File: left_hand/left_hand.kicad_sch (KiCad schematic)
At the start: 43 parts, among them J1 Conn_01x08, J2 Screw_Terminal_01x10, J3 8P8C_Shielded, J4 Conn_02x02_Top_Bottom, J7 Conn_01x02, J8 Conn_01x02, M1 Motor_Servo, M2 Motor_Servo, M3 Motor_Servo, M4 Motor_Servo, M5 Motor_Servo, Q1 Q_NMOS_GDS, Q2 Q_NMOS_GDS, Q3 Q_NMOS_GDS, Q4 Q_NMOS_GDS, Q5 Q_NMOS_GDS, U1 MCP23017_SP, U2 PCA9685PW

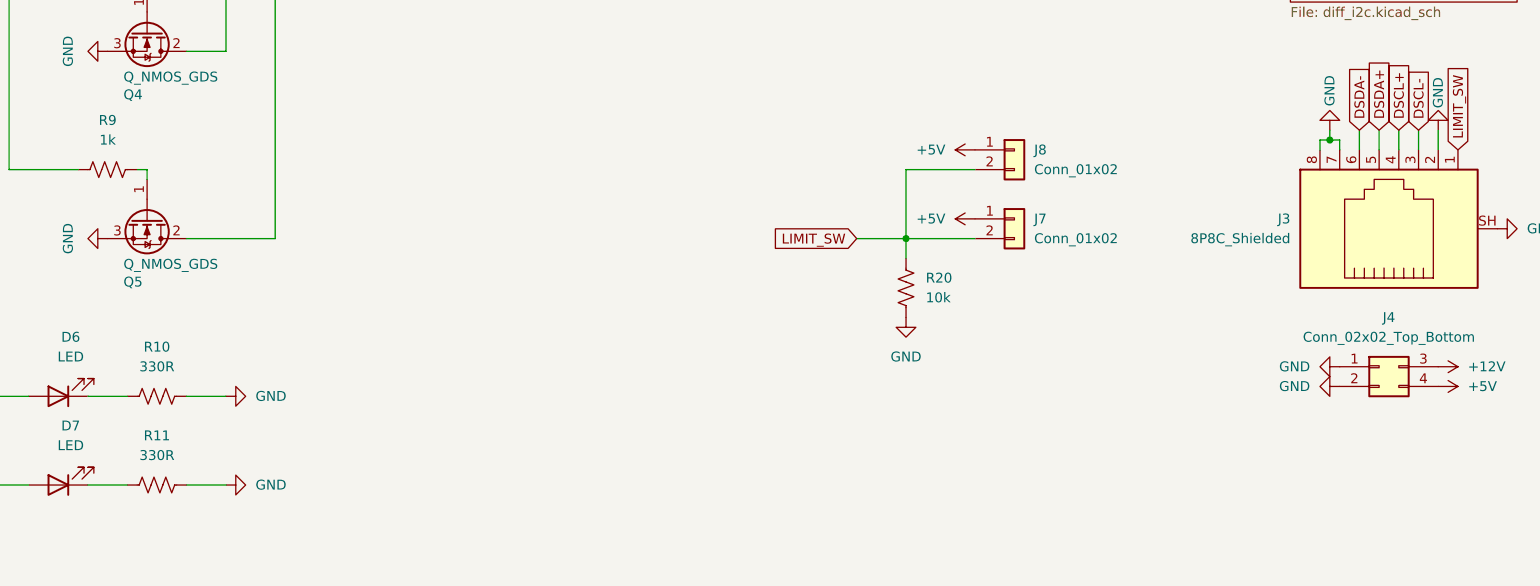
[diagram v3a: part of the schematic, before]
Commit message: Added screw terminals etc for both stepper drivers
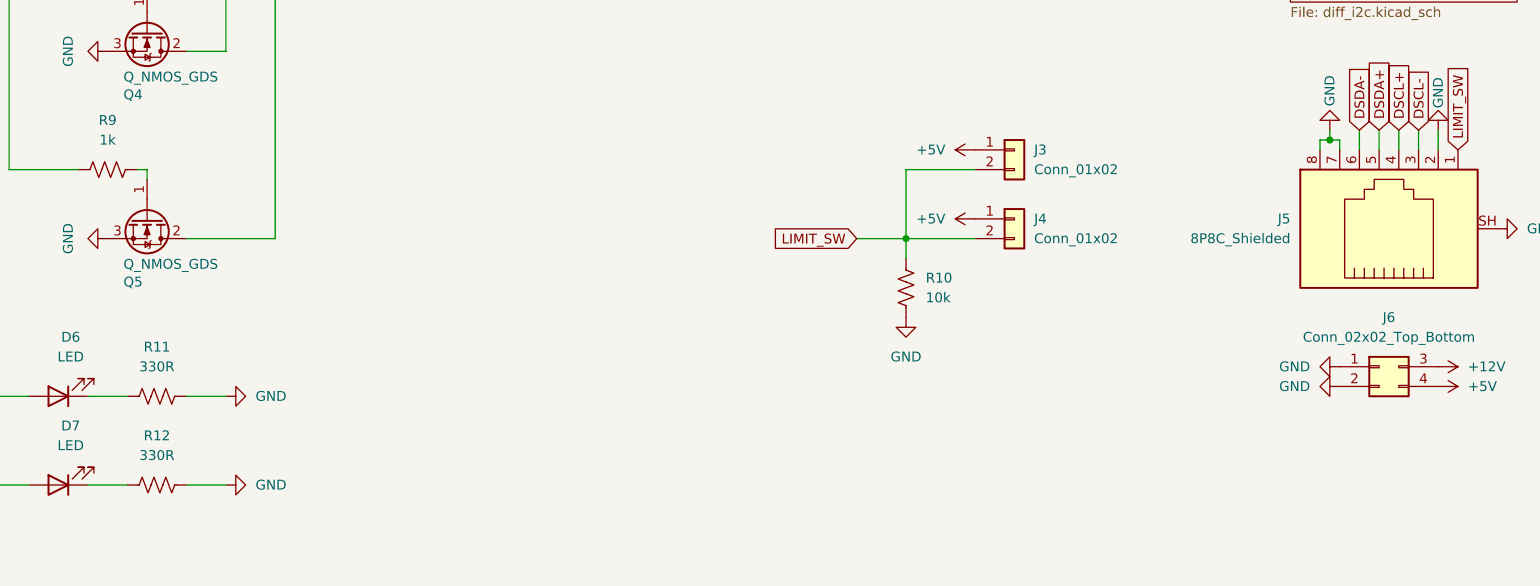
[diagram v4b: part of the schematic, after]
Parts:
- renumbered J8 to J3, J7 to J4, J3 to J5, J4 to J6, R20 to R10, R10 to R11, R11 to R12
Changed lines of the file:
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@@
 		(dnp no)
 		(fields_autoplaced yes)
-		(property "Reference" "#PWR036"
+		(property "Reference" "#PWR037"
 			(at 279.4 138.43 0)
 			(effects
@@
 			(project ""
 				(path "/22d0e2d6-ca63-4bde-b22b-39e933f56b8a"
-					(reference "#PWR036")
+					(reference "#PWR037")
 					(unit 1)
 				)
@@
 		(dnp no)
 		(fields_autoplaced yes)
-		(property "Reference" "#PWR021"
+		(property "Reference" "#PWR022"
 			(at 156.21 74.93 0)
 			(effects
@@
 			(project "left_hand"
 				(path "/22d0e2d6-ca63-4bde-b22b-39e933f56b8a"
-					(reference "#PWR021")
+					(reference "#PWR022")
 					(unit 1)
 				)
@@
 		(dnp no)
 		(fields_autoplaced yes)
-		(property "Reference" "#PWR055"
+		(property "Reference" "#PWR036"
 			(at 209.55 137.16 0)
 			(effects
@@
 			(project "left_hand"
 				(path "/22d0e2d6-ca63-4bde-b22b-39e933f56b8a"
-					(reference "#PWR055")
+					(reference "#PWR036")
 					(unit 1)
 				)
@@
 		(dnp no)
 		(fields_autoplaced yes)
-		(property "Reference" "#PWR040"
+		(property "Reference" "#PWR042"
 			(at 246.38 158.75 0)
 			(effects
@@
 			(project "left_hand"
 				(path "/22d0e2d6-ca63-4bde-b22b-39e933f56b8a"
-					(reference "#PWR040")
+					(reference "#PWR042")
 					(unit 1)
 				)
@@
 		(dnp no)
 		(fields_autoplaced yes)
-		(property "Reference" "J4"
+		(property "Reference" "J6"
 			(at 259.08 149.86 0)
 			(effects
@@
 			(project "left_hand"
 				(path "/22d0e2d6-ca63-4bde-b22b-39e933f56b8a"
-					(reference "J4")
+					(reference "J6")
 					(unit 1)
 				)
@@
 		(dnp no)
 		(fields_autoplaced yes)
-		(property "Reference" "#PWR038"
+		(property "Reference" "#PWR041"
 			(at 261.62 156.21 0)
 			(effects
@@
 			(project ""
 				(path "/22d0e2d6-ca63-4bde-b22b-39e933f56b8a"
-					(reference "#PWR038")
+					(reference "#PWR041")
 					(unit 1)
 				)
@@
 		(dnp no)
 		(fields_autoplaced yes)
-		(property "Reference" "#PWR057"
+		(property "Reference" "#PWR035"
 			(at 209.55 128.27 0)
 			(effects
@@
 			(project "left_hand"
 				(path "/22d0e2d6-ca63-4bde-b22b-39e933f56b8a"
-					(reference "#PWR057")
+					(reference "#PWR035")
 					(unit 1)
 				)
@@
 		(dnp no)
 		(fields_autoplaced yes)
-		(property "Reference" "#PWR023"
+		(property "Reference" "#PWR024"
 			(at 171.45 78.74 0)
 			(effects
@@
 			(project ""
 				(path "/22d0e2d6-ca63-4bde-b22b-39e933f56b8a"
-					(reference "#PWR023")
+					(reference "#PWR024")
 					(unit 1)
 				)
@@
 		(dnp no)
 		(fields_autoplaced yes)
-		(property "Reference" "R11"
+		(property "Reference" "R12"
 			(at 100.33 165.1 90)
 			(effects
@@
 			(project "left_hand"
 				(path "/22d0e2d6-ca63-4bde-b22b-39e933f56b8a"
-					(reference "R11")
+					(reference "R12")
 					(unit 1)
 				)
@@
 		(dnp no)
 		(fields_autoplaced yes)
-		(property "Reference" "#PWR035"
+		(property "Reference" "#PWR038"
 			(at 87.63 139.7 0)
 			(effects
@@
 			(project "left_hand"
 				(path "/22d0e2d6-ca63-4bde-b22b-39e933f56b8a"
-					(reference "#PWR035")
+					(reference "#PWR038")
 					(unit 1)
 				)
@@
 		(dnp no)
 		(fields_autoplaced yes)
-		(property "Reference" "J3"
+		(property "Reference" "J5"
 			(at 246.38 137.1599 90)
 			(effects
@@
 			(project ""
 				(path "/22d0e2d6-ca63-4bde-b22b-39e933f56b8a"
-					(reference "J3")
+					(reference "J5")
 					(unit 1)
 				)
@@
 		(dnp no)
 		(fields_autoplaced yes)
-		(property "Reference" "#PWR039"
+		(property "Reference" "#PWR044"
 			(at 115.57 160.02 0)
 			(effects
@@
 			(project "left_hand"
 				(path "/22d0e2d6-ca63-4bde-b22b-39e933f56b8a"
-					(reference "#PWR039")
+					(reference "#PWR044")
 					(unit 1)
 				)
@@
 		(dnp no)
 		(fields_autoplaced yes)
-		(property "Reference" "#PWR037"
+		(property "Reference" "#PWR040"
 			(at 246.38 156.21 0)
 			(effects
@@
 			(project "left_hand"
 				(path "/22d0e2d6-ca63-4bde-b22b-39e933f56b8a"
-					(reference "#PWR037")
+					(reference "#PWR040")
 					(unit 1)
 				)
@@
 		(dnp no)
 		(fields_autoplaced yes)
-		(property "Reference" "#PWR020"
+		(property "Reference" "#PWR021"
 			(at 87.63 67.31 0)
 			(effects
@@
 			(project "left_hand"
 				(path "/22d0e2d6-ca63-4bde-b22b-39e933f56b8a"
-					(reference "#PWR020")
+					(reference "#PWR021")
 					(unit 1)
 				)
@@
 		(on_board yes)
 		(dnp no)
-		(property "Reference" "#PWR042"
+		(property "Reference" "#PWR045"
 			(at 115.57 171.45 0)
 			(effects
@@
 			(project "left_hand"
 				(path "/22d0e2d6-ca63-4bde-b22b-39e933f56b8a"
-					(reference "#PWR042")
+					(reference "#PWR045")
 					(unit 1)
 				)
@@
 		(dnp no)
 		(fields_autoplaced yes)
-		(property "Reference" "R10"
+		(property "Reference" "R11"
 			(at 100.33 153.67 90)
 			(effects
@@
 			(project "left_hand"
 				(path "/22d0e2d6-ca63-4bde-b22b-39e933f56b8a"
-					(reference "R10")
+					(reference "R11")
 					(unit 1)
 				)
@@
 		(dnp no)
 		(fields_autoplaced yes)
-		(property "Reference" "#PWR022"
+		(property "Reference" "#PWR023"
 			(at 163.83 64.77 0)
 			(effects
@@
 			(project "left_hand"
 				(path "/22d0e2d6-ca63-4bde-b22b-39e933f56b8a"
-					(reference "#PWR022")
+					(reference "#PWR023")
 					(unit 1)
 				)
@@
 		(dnp no)
 		(fields_autoplaced yes)
-		(property "Reference" "#PWR056"
+		(property "Reference" "#PWR039"
 			(at 196.85 156.21 0)
 			(effects
@@
 			(project "left_hand"
 				(path "/22d0e2d6-ca63-4bde-b22b-39e933f56b8a"
-					(reference "#PWR056")
+					(reference "#PWR039")
 					(unit 1)
 				)
@@
 		(dnp no)
 		(fields_autoplaced yes)
-		(property "Reference" "J8"
+		(property "Reference" "J3"
 			(at 213.36 128.2699 0)
 			(effects
@@
 			(project "left_hand"
 				(path "/22d0e2d6-ca63-4bde-b22b-39e933f56b8a"
-					(reference "J8")
+					(reference "J3")
 					(unit 1)
 				)
@@
 		(dnp no)
 		(fields_autoplaced yes)
-		(property "Reference" "J7"
+		(property "Reference" "J4"
 			(at 213.36 137.1599 0)
 			(effects
@@
 			(project "left_hand"
 				(path "/22d0e2d6-ca63-4bde-b22b-39e933f56b8a"
-					(reference "J7")
+					(reference "J4")
 					(unit 1)
 				)
@@
 		(dnp no)
 		(fields_autoplaced yes)
-		(property "Reference" "R20"
+		(property "Reference" "R10"
 			(at 199.39 144.7799 0)
 			(effects
@@
 			(project "left_hand"
 				(path "/22d0e2d6-ca63-4bde-b22b-39e933f56b8a"
-					(reference "R20")
+					(reference "R10")
 					(unit 1)
 				)
@@
 		(on_board yes)
 		(dnp no)
-		(property "Reference" "#PWR024"
+		(property "Reference" "#PWR020"
 			(at 24.13 67.31 0)
 			(effects
@@
 			(project ""
 				(path "/22d0e2d6-ca63-4bde-b22b-39e933f56b8a"
-					(reference "#PWR024")
+					(reference "#PWR020")
 					(unit 1)
 				)
@@
 		(dnp no)
 		(fields_autoplaced yes)
-		(property "Reference" "#PWR041"
+		(property "Reference" "#PWR043"
 			(at 261.62 158.75 0)
 			(effects
@@
 			(project "left_hand"
 				(path "/22d0e2d6-ca63-4bde-b22b-39e933f56b8a"
-					(reference "#PWR041")
+					(reference "#PWR043")
 					(unit 1)
 				)

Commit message: Started layout of control board
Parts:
- added R9: 10k, Resistor_THT:R_Axial_DIN0207_L6.3mm_D2.5mm_P10.16mm_Horizontal, symbol Device:R_US
- renumbered R9 to R10, R10 to R11, R11 to R12, R12 to R13
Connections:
- net GND: now also R9.1; no longer J5.8
- net LIMIT_SW renamed LIMIT_SW_L
- net LIMIT_SW_L: no longer J3.2 (Pin_2)
- new net LIMIT_SW_R: J3.2 (Pin_2), J5.8, R9.2
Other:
- moved on the sheet: J3

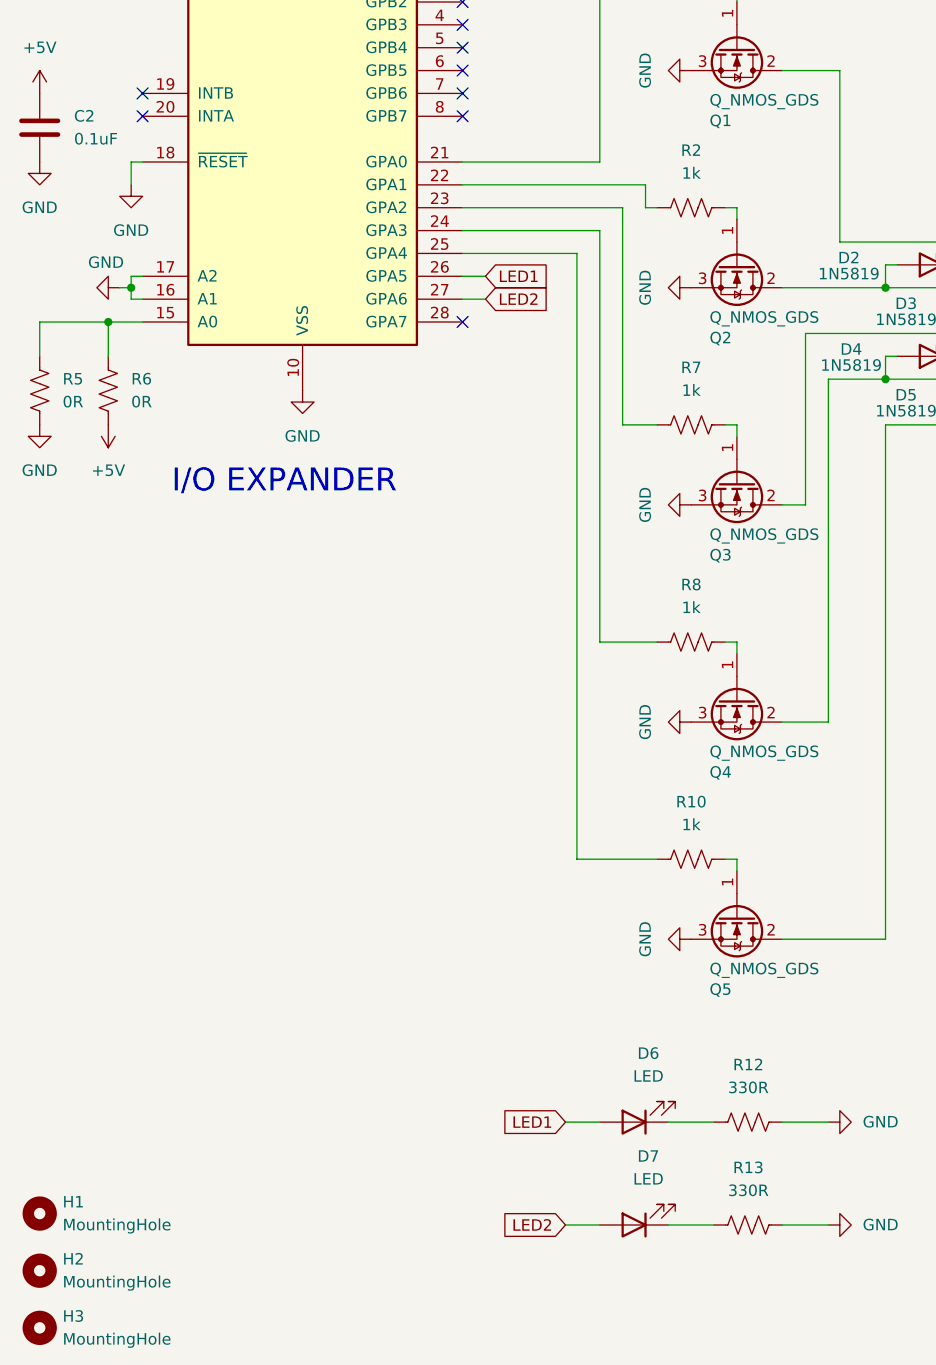
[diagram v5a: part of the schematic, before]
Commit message: Version 1 AS-BUILT commit
This commit has the schematics of version 1 of the system AS IT WAS BUILT
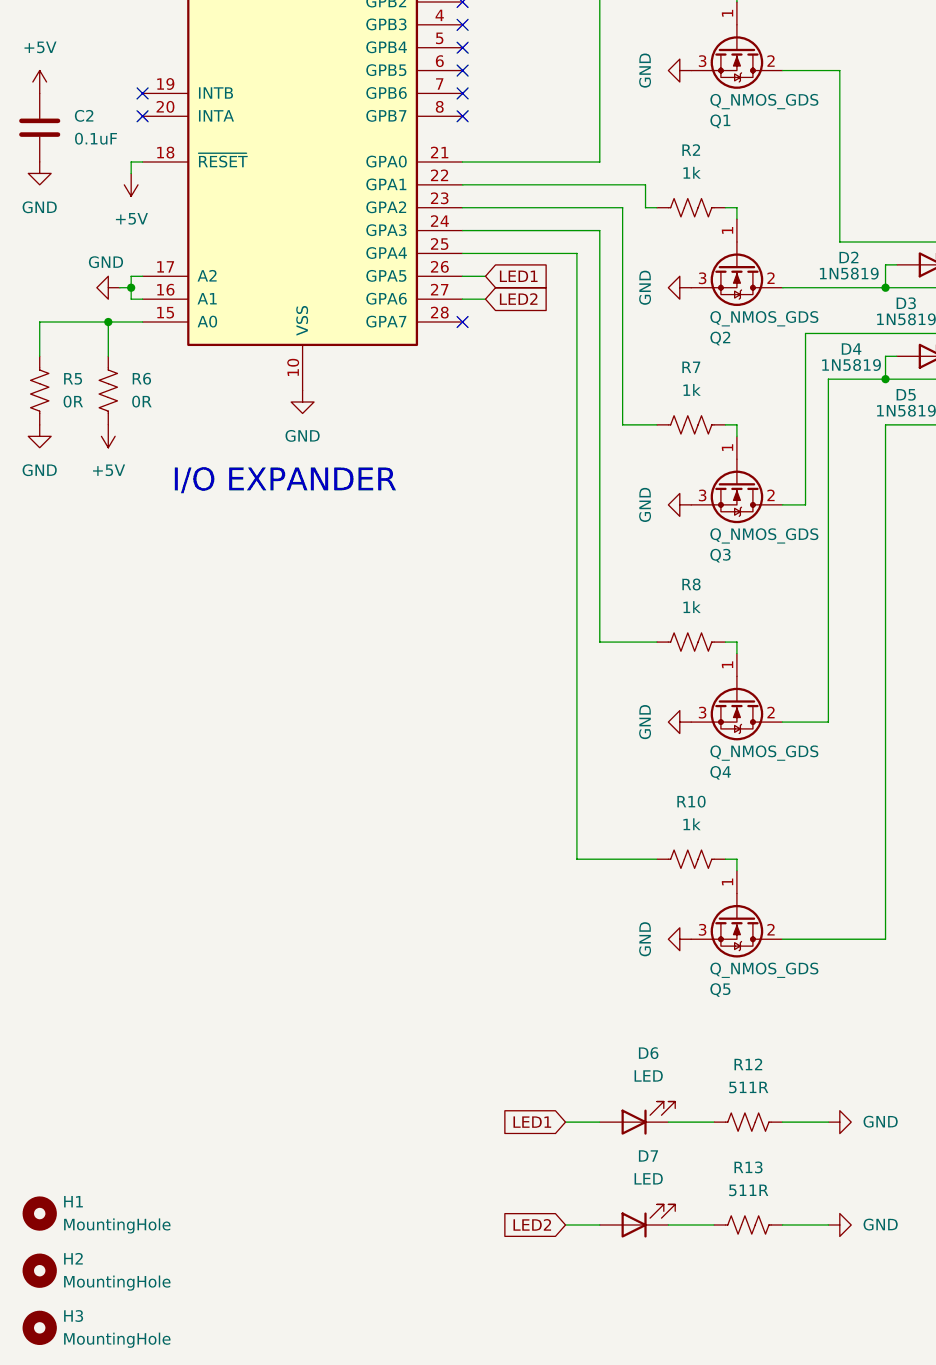
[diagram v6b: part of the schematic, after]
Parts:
- R12, R13: value 330R -> 511R
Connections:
- net +5V: now also U1.18 (~{RESET})
- net GND: no longer U1.18 (~{RESET})
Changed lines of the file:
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@@
 	(wire
 		(pts
-			(xy 31.75 55.88) (xy 31.75 53.34)
-		)
-		(stroke
-			(width 0)
-			(type default)
-		)
-	)
-	(wire
-		(pts
 			(xy 248.92 45.72) (xy 238.76 45.72)
 		)
@@
 	(wire
 		(pts
-			(xy 31.75 53.34) (xy 33.02 53.34)
-		)
-		(stroke
-			(width 0)
-			(type default)
-		)
-	)
-	(wire
-		(pts
 			(xy 171.45 66.04) (xy 173.99 66.04)
 		)
@@
 	(wire
 		(pts
+			(xy 31.75 53.34) (xy 33.02 53.34)
+		)
+		(stroke
+			(width 0)
+			(type default)
+		)
+	)
+	(wire
+		(pts
 			(xy 80.01 160.02) (xy 83.82 160.02)
 		)
@@
 	(wire
 		(pts
+			(xy 31.75 54.61) (xy 31.75 53.34)
+		)
+		(stroke
+			(width 0)
+			(type default)
+		)
+	)
+	(wire
+		(pts
 			(xy 110.49 43.18) (xy 110.49 62.23)
 		)
@@
 			)
 		)
-		(property "Value" "330R"
+		(property "Value" "511R"
 			(at 100.33 167.64 90)
 			(effects
@@
 	(symbol
 		(lib_id "power:+5V")
+		(at 31.75 54.61 180)
+		(unit 1)
+		(exclude_from_sim no)
+		(in_bom yes)
+		(on_board yes)
+		(dnp no)
+		(fields_autoplaced yes)
+		(property "Reference" "#PWR017"
+			(at 31.75 50.8 0)
+			(effects
+				(font
+					(size 1.27 1.27)
+				)
+				(hide yes)
+			)
+		)
+		(property "Value" "+5V"
+			(at 31.75 59.69 0)
+			(effects
+				(font
+					(size 1.27 1.27)
+				)
+			)
+		)
+		(property "Footprint" ""
+			(at 31.75 54.61 0)
+			(effects
+				(font
+					(size 1.27 1.27)
+				)
+				(hide yes)
+			)
+		)
+		(property "Datasheet" ""
+			(at 31.75 54.61 0)
+			(effects
+				(font
+					(size 1.27 1.27)
+				)
+				(hide yes)
+			)
+		)
+		(property "Description" "Power symbol creates a global label with name \"+5V\""
+			(at 31.75 54.61 0)
+			(effects
+				(font
+					(size 1.27 1.27)
+				)
+				(hide yes)
+			)
+		)
+		(pin "1"
+		)
+		(instances
+			(project "left_hand"
+				(path "/22d0e2d6-ca63-4bde-b22b-39e933f56b8a"
+					(reference "#PWR017")
+					(unit 1)
+				)
+			)
+		)
+	)
+	(symbol
+		(lib_id "power:+5V")
 		(at 191.77 27.94 0)
 		(unit 1)
@@
 			)
 		)
-		(property "Value" "330R"
+		(property "Value" "511R"
 			(at 100.33 156.21 90)
 			(effects
@@
 					(unit 1)
 				)
-			)
-		)
-	)
-	(symbol
-		(lib_id "power:GND")
-		(at 31.75 55.88 0)
-		(unit 1)
-		(exclude_from_sim no)
-		(in_bom yes)
-		(on_board yes)
-		(dnp no)
-		(fields_autoplaced yes)
-		(property "Reference" "#PWR017"
-			(at 31.75 62.23 0)
-			(effects
-				(font
-					(size 1.27 1.27)
-				)
-				(hide yes)
-			)
-		)
-		(property "Value" "GND"
-			(at 31.75 60.96 0)
-			(effects
-				(font
-					(size 1.27 1.27)
-				)
-			)
-		)
-		(property "Footprint" ""
-			(at 31.75 55.88 0)
-			(effects
-				(font
-					(size 1.27 1.27)
-				)
-				(hide yes)
-			)
-		)
-		(property "Datasheet" ""
-			(at 31.75 55.88 0)
-			(effects
-				(font
-					(size 1.27 1.27)
-				)
-				(hide yes)
-			)
-		)
-		(property "Description" "Power symbol creates a global label with name \"GND\" , ground"
-			(at 31.75 55.88 0)
-			(effects
-				(font
-					(size 1.27 1.27)
-				)
-				(hide yes)
-			)
-		)
-		(pin "1"
-		)
-		(instances
-			(project ""
-				(path "/22d0e2d6-ca63-4bde-b22b-39e933f56b8a"
-					(reference "#PWR017")
-					(unit 1)
-				)

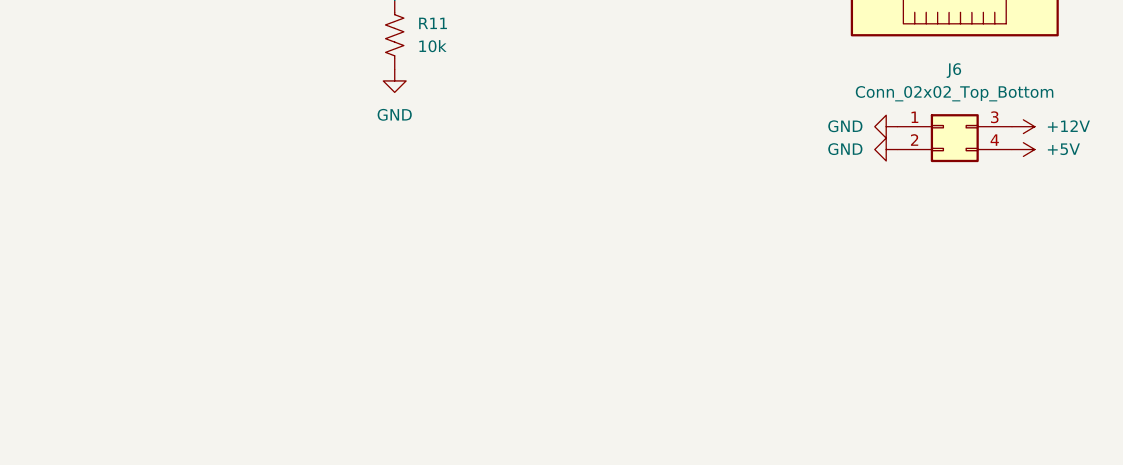
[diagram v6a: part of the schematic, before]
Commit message: Added drawing information boxes
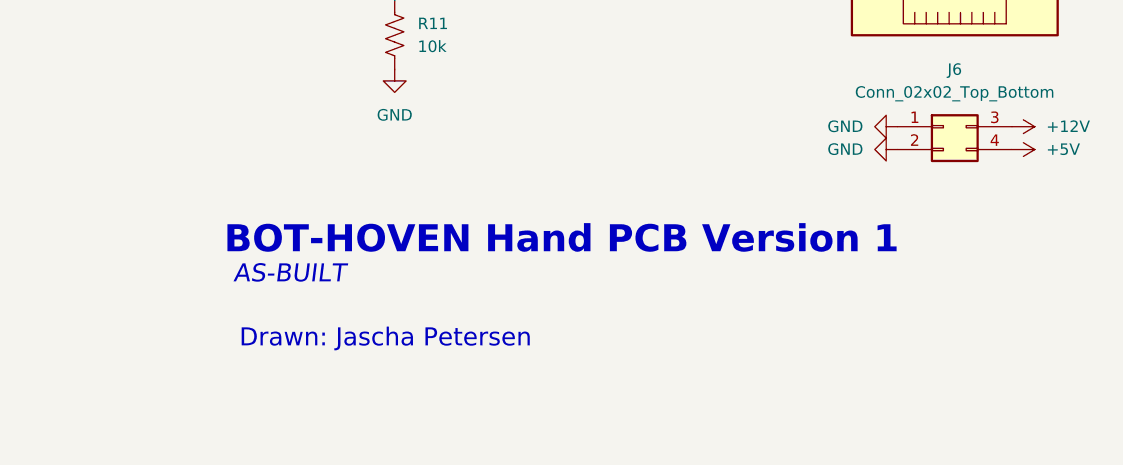
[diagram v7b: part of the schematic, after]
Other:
- note added: "AS-BUILT"
- note added: "BOT-HOVEN Hand PCB Version 1"
- note added: "Drawn: Jascha Petersen"
- title: (none) -> Hand PCB Main
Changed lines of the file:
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@@
 	(generator_version "8.0")
 	(paper "A4")
+	(title_block
+		(title "Hand PCB Main")
+	)
 	(junction
 		(at 196.85 139.7)
@@
 		)
 	)
+	(text "BOT-HOVEN Hand PCB Version 1"
+		(exclude_from_sim no)
+		(at 215.392 168.91 0)
+		(effects
+			(font
+				(size 3 3)
+				(thickness 0.6)
+				(bold yes)
+			)
+		)
+	)
 	(text "I/O EXPANDER"
 		(exclude_from_sim no)
@@
 			)
 		)
+	)
+	(text "Drawn: Jascha Petersen"
+		(exclude_from_sim no)
+		(at 195.834 179.832 0)
+		(effects
+			(font
+				(size 2 2)
+			)
+		)
+	)
+	(text "AS-BUILT"
+		(exclude_from_sim no)
+		(at 185.166 172.72 0)
+		(effects
+			(font
+				(size 2 2)
+				(italic yes)
+			)
+		)
